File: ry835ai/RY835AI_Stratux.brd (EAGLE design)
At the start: 65 x 56 mm, 9 parts, among them X2 RASPI_BOARD_B+#_HD

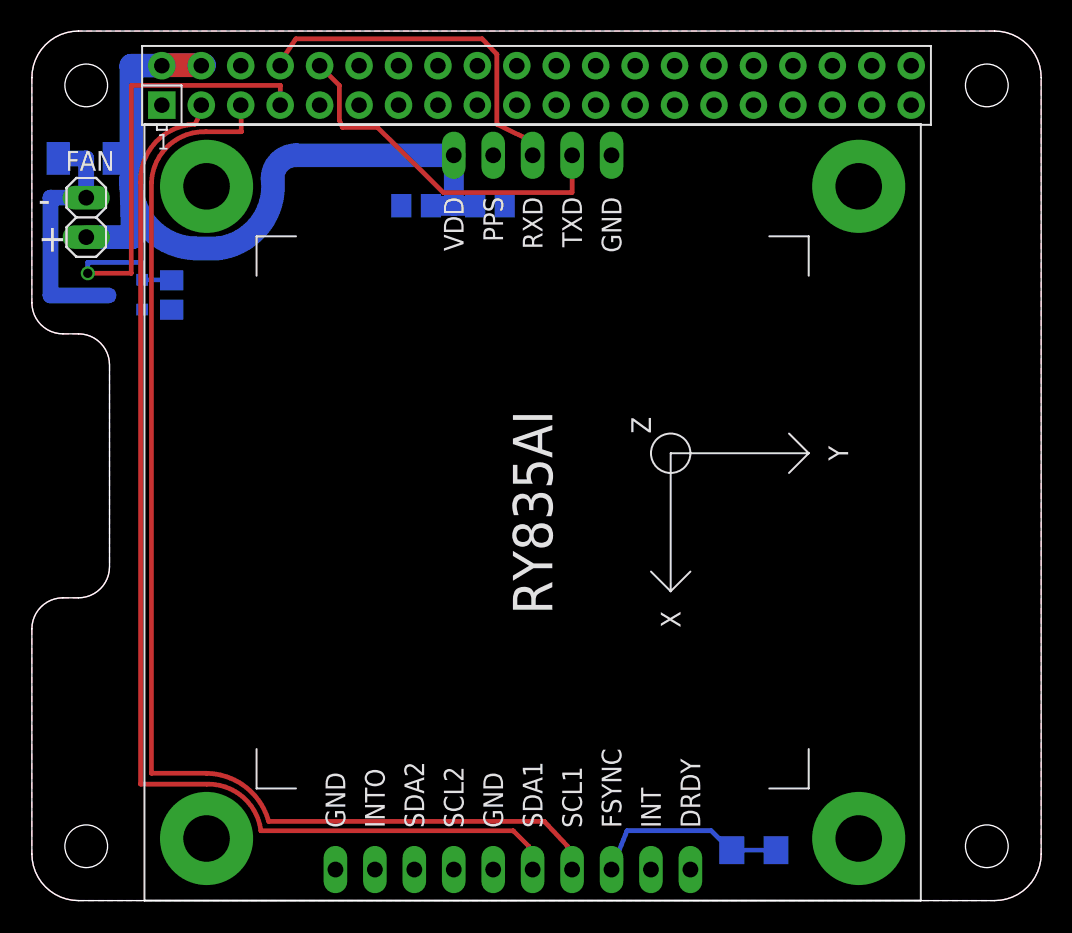
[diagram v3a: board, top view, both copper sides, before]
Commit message: Revised board design with provisions for FAN & PWR_IN.
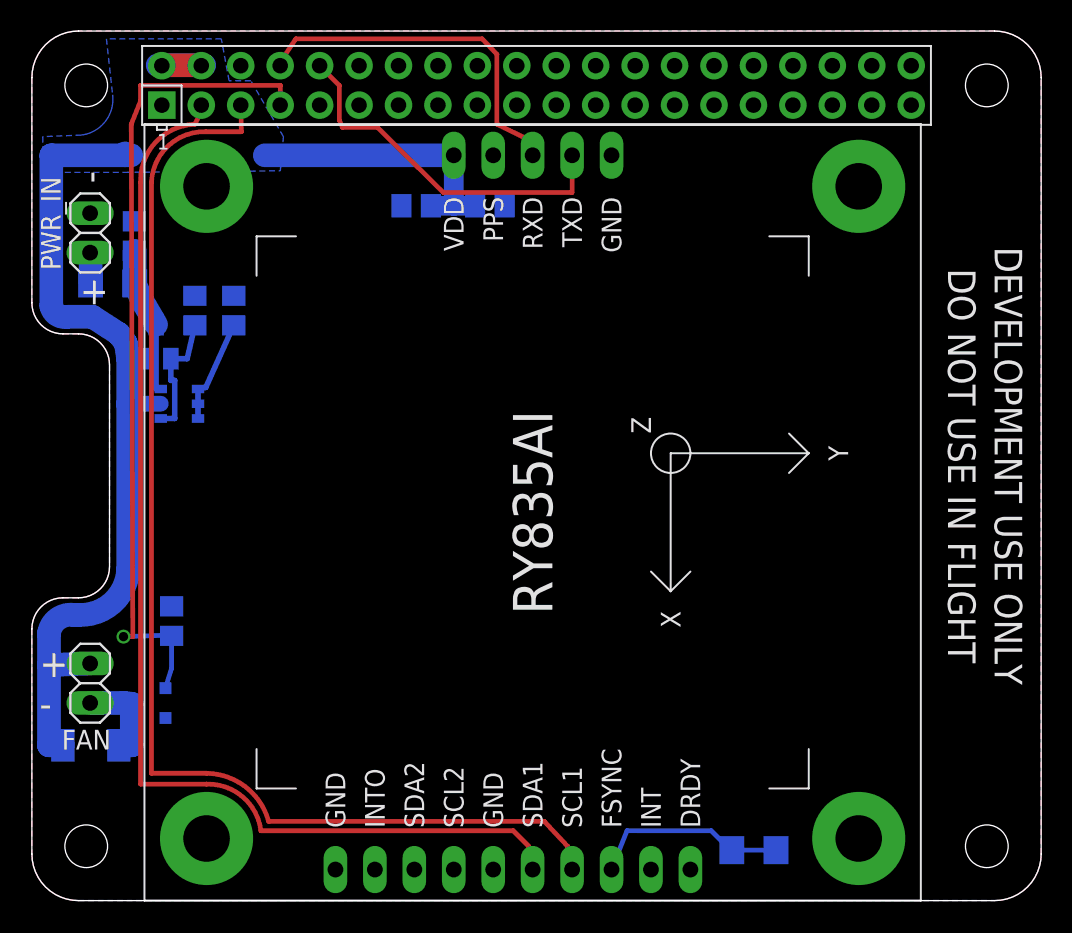
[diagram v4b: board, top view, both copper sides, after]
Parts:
- added C3: 1uF, rcl:C0805
- added F1: 1206L110SLYR, jblib:R1206
- added PWR_IN: (no value), pinhead:1X02
- added R2, R3: 47k 1%, resistor:R0805
- added U$2: DMG2305UX, jblib:SOT23
- added U$3: DMMT5401, jblib:SOT26
- moved D1 37.8 mm to (3.80, 10.0), turned to 180 degrees
- moved FAN 30.0 mm to (3.75, 14.0), turned to 270 degrees
- moved Q1 26.3 mm to (7.50, 12.7)
- moved R1 21.0 mm to (9.00, 18.0), turned to 270 degrees
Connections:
- new net N$10: R3.2, U$2.1, U$3.4
- new net N$6: F1.1, PWR_IN.2
- new net N$7: C3.1, F1.2, U$2.3, U$3.6
- new net N$9: R2.2, U$3.1, U$3.2, U$3.3
- net +5V: now also U$2.2, U$3.5
- net GND: now also C3.2, PWR_IN.1, R2.1, R3.1
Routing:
- net +5V: track 54.3 -> 79.5 mm
- net FAN_GPIO: track 33.0 -> 53.1 mm
- net N$7: track 0.00 -> 11.7 mm
- net N$4: track 16.7 -> 6.19 mm
- net N$10: track 0.00 -> 8.26 mm
- net N$9: track 0.00 -> 6.80 mm
- net N$6: track 0.00 -> 2.01 mm
- added copper zone on layer 16, net +5V
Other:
- board text added: "DEVELOPMENT USE ONLY"
- board text added: "DO NOT USE IN FLIGHT"
- board text added: "v0.4"

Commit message: Minor change R1=10k
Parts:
- R1: value (none) -> 10k
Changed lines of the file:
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@@
 <grid distance="0.500000001" unitdist="mm" unit="mm" style="lines" multiple="1" display="no" altdistance="0.1" altunitdist="mm" altunit="mm"/>
 <layers>
-<layer number="1" name="Top" color="4" fill="1" visible="no" active="yes"/>
+<layer number="1" name="Top" color="4" fill="1" visible="yes" active="yes"/>
 <layer number="16" name="Bottom" color="1" fill="1" visible="yes" active="yes"/>
 <layer number="17" name="Pads" color="2" fill="1" visible="yes" active="yes"/>
@@
 <layer number="19" name="Unrouted" color="6" fill="1" visible="yes" active="yes"/>
 <layer number="20" name="Dimension" color="15" fill="1" visible="yes" active="yes"/>
-<layer number="21" name="tPlace" color="7" fill="1" visible="no" active="yes"/>
+<layer number="21" name="tPlace" color="7" fill="1" visible="yes" active="yes"/>
 <layer number="22" name="bPlace" color="7" fill="1" visible="yes" active="yes"/>
-<layer number="23" name="tOrigins" color="15" fill="1" visible="no" active="yes"/>
+<layer number="23" name="tOrigins" color="15" fill="1" visible="yes" active="yes"/>
 <layer number="24" name="bOrigins" color="15" fill="1" visible="yes" active="yes"/>
-<layer number="25" name="tNames" color="7" fill="1" visible="no" active="yes"/>
+<layer number="25" name="tNames" color="7" fill="1" visible="yes" active="yes"/>
 <layer number="26" name="bNames" color="7" fill="1" visible="yes" active="yes"/>
 <layer number="27" name="tValues" color="7" fill="1" visible="no" active="yes"/>
 <layer number="28" name="bValues" color="7" fill="1" visible="no" active="yes"/>
 <layer number="29" name="tStop" color="7" fill="3" visible="no" active="yes"/>
-<layer number="30" name="bStop" color="7" fill="6" visible="yes" active="yes"/>
+<layer number="30" name="bStop" color="7" fill="6" visible="no" active="yes"/>
 <layer number="31" name="tCream" color="7" fill="4" visible="no" active="yes"/>
 <layer number="32" name="bCream" color="7" fill="5" visible="no" active="yes"/>
@@
 <layer number="49" name="Reference" color="7" fill="1" visible="no" active="yes"/>
 <layer number="50" name="dxf" color="7" fill="1" visible="no" active="yes"/>
-<layer number="51" name="tDocu" color="7" fill="1" visible="no" active="yes"/>
-<layer number="52" name="bDocu" color="7" fill="1" visible="no" active="yes"/>
+<layer number="51" name="tDocu" color="7" fill="1" visible="yes" active="yes"/>
+<layer number="52" name="bDocu" color="7" fill="1" visible="yes" active="yes"/>
 <layer number="53" name="tGND_GNDA" color="7" fill="9" visible="no" active="no"/>
 <layer number="54" name="bGND_GNDA" color="1" fill="9" visible="no" active="no"/>
@@
 <attribute name="VALUE" x="0.575" y="16.54" size="1.27" layer="27" rot="R270"/>
 </element>
-<element name="R1" library="resistor" package="R0805" value="" x="9" y="18" smashed="yes" rot="MR270">
+<element name="R1" library="resistor" package="R0805" value="10k" x="9" y="18" smashed="yes" rot="MR270">
 <attribute name="NAME" x="10.065" y="18.43" size="0.8128" layer="26" rot="MR180"/>
 <attribute name="VALUE" x="11.54" y="18.635" size="1.27" layer="28" rot="MR270"/>

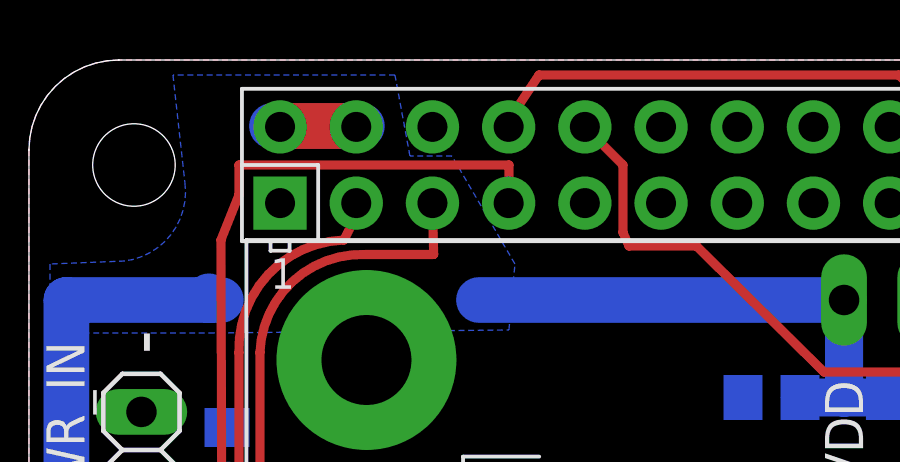
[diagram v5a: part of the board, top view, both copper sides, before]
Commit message: Modified fan control signal to use GPIO18 rather than GPIO4. This is consistent with currently used AHRS boards. This revision has not been manufactured or tested, so make sure to DRC and double check if you decide to have this made.
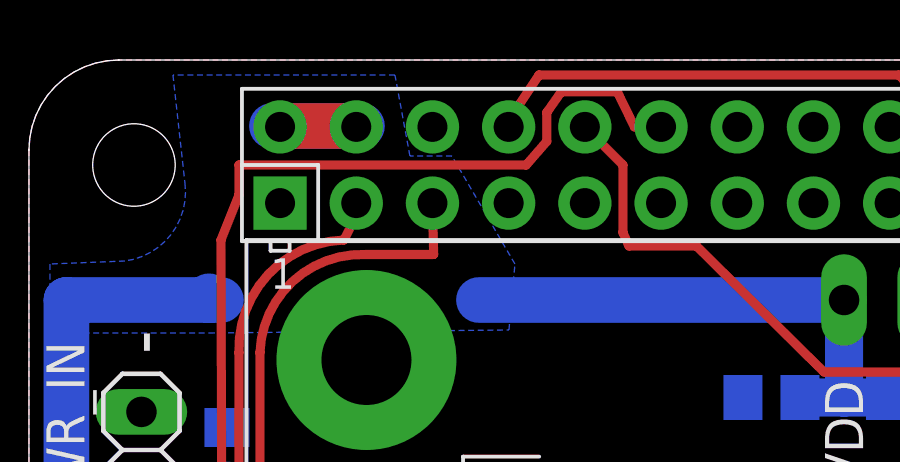
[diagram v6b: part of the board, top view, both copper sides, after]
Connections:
- net FAN_GPIO: now also X2.12; no longer X2.7
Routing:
- net FAN_GPIO: track 53.1 -> 59.3 mm
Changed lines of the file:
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@@
 <?xml version="1.0" encoding="utf-8"?>
 <!DOCTYPE eagle SYSTEM "eagle.dtd">
-<eagle version="7.2.0">
+<eagle version="8.2.1">
 <drawing>
 <settings>
@@
 <setting verticaltext="up"/>
 </settings>
-<grid distance="0.500000001" unitdist="mm" unit="mm" style="lines" multiple="1" display="no" altdistance="0.1" altunitdist="mm" altunit="mm"/>
+<grid distance="0.5" unitdist="mm" unit="mm" style="lines" multiple="1" display="no" altdistance="0.1" altunitdist="mm" altunit="mm"/>
 <layers>
-<layer number="1" name="Top" color="4" fill="1" visible="yes" active="yes"/>
+<layer number="1" name="Top" color="4" fill="1" visible="no" active="yes"/>
 <layer number="16" name="Bottom" color="1" fill="1" visible="yes" active="yes"/>
 <layer number="17" name="Pads" color="2" fill="1" visible="yes" active="yes"/>
 <layer number="18" name="Vias" color="2" fill="1" visible="yes" active="yes"/>
-<layer number="19" name="Unrouted" color="6" fill="1" visible="yes" active="yes"/>
+<layer number="19" name="Unrouted" color="6" fill="1" visible="no" active="yes"/>
 <layer number="20" name="Dimension" color="15" fill="1" visible="yes" active="yes"/>
-<layer number="21" name="tPlace" color="7" fill="1" visible="yes" active="yes"/>
+<layer number="21" name="tPlace" color="7" fill="1" visible="no" active="yes"/>
 <layer number="22" name="bPlace" color="7" fill="1" visible="yes" active="yes"/>
-<layer number="23" name="tOrigins" color="15" fill="1" visible="yes" active="yes"/>
+<layer number="23" name="tOrigins" color="15" fill="1" visible="no" active="yes"/>
 <layer number="24" name="bOrigins" color="15" fill="1" visible="yes" active="yes"/>
-<layer number="25" name="tNames" color="7" fill="1" visible="yes" active="yes"/>
+<layer number="25" name="tNames" color="7" fill="1" visible="no" active="yes"/>
 <layer number="26" name="bNames" color="7" fill="1" visible="yes" active="yes"/>
 <layer number="27" name="tValues" color="7" fill="1" visible="no" active="yes"/>
@@
 <layer number="49" name="Reference" color="7" fill="1" visible="no" active="yes"/>
 <layer number="50" name="dxf" color="7" fill="1" visible="no" active="yes"/>
-<layer number="51" name="tDocu" color="7" fill="1" visible="yes" active="yes"/>
-<layer number="52" name="bDocu" color="7" fill="1" visible="yes" active="yes"/>
+<layer number="51" name="tDocu" color="7" fill="1" visible="no" active="yes"/>
+<layer number="52" name="bDocu" color="7" fill="1" visible="no" active="yes"/>
 <layer number="53" name="tGND_GNDA" color="7" fill="9" visible="no" active="no"/>
 <layer number="54" name="bGND_GNDA" color="1" fill="9" visible="no" active="no"/>
@@
 <signal name="FAN_GPIO">
 <contactref element="Q1" pad="1"/>
-<contactref element="X2" pad="7"/>
 <contactref element="R1" pad="2"/>
-<wire x1="15.99" y1="51.23" x2="16" y2="51.23" width="0.3048" layer="1"/>
-<wire x1="16" y1="51.23" x2="16" y2="52.5" width="0.3048" layer="1"/>
-<wire x1="16" y1="52.5" x2="7" y2="52.5" width="0.3048" layer="1"/>
-<wire x1="7" y1="52.5" x2="7" y2="51.5" width="0.3048" layer="1"/>
+<wire x1="7" y1="51.5" x2="7" y2="52.5" width="0.3048" layer="1"/>
 <wire x1="7" y1="51.5" x2="6.4" y2="50" width="0.3048" layer="1"/>
 <wire x1="6.4" y1="50" x2="6.5" y2="17" width="0.3048" layer="1"/>
@@
 <wire x1="5.9" y1="17" x2="9" y2="17.1" width="0.3048" layer="16"/>
 <wire x1="9" y1="17.1" x2="9" y2="17.05" width="0.3048" layer="16"/>
+<contactref element="X2" pad="12"/>
+<wire x1="17.2616" y1="53.28603125" x2="17.2616" y2="54.25396875" width="0.3048" layer="1"/>
+<wire x1="17.2616" y1="54.25396875" x2="17.74603125" y2="54.9384" width="0.3048" layer="1"/>
+<wire x1="17.74603125" y1="54.9384" x2="19.61396875" y2="54.9384" width="0.3048" layer="1"/>
+<wire x1="16.57556875" y1="52.5" x2="17.2616" y2="53.28603125" width="0.3048" layer="1"/>
+<wire x1="19.61396875" y1="54.9384" x2="20.18236875" y2="53.77" width="0.3048" layer="1"/>
+<wire x1="20.18236875" y1="53.77" x2="21.07" y2="53.77" width="0.3048" layer="1"/>
+<wire x1="7" y1="52.5" x2="16.57556875" y2="52.5" width="0.3048" layer="1"/>
 </signal>
 <signal name="N$4">
